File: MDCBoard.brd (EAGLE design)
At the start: 43.9 x 32.6 mm, 200 parts, among them J1 JUMPER-SOLDER, J10 MICROSD-SOCKET, J11 USB-C-RECEPTACLE-KOREANHRO, J2 JUMPER-SOLDER, J3 JUMPER-SOLDER, J4 JUMPER-SOLDER, J5 JST-SM02B-SRSS-TB, J6 JUMPER-SOLDER, J7 JUMPER-SOLDER, J8 JUMPER-SOLDER, Q1 PMOS-NEXPERIA-SOT1220, Q2 PMOS-NEXPERIA-SOT1220, Q3 PMOS-NEXPERIA-SOT1220, Q4 DIODESINC-DMG2305UX, Q5 DIODESINC-DMG2305UX, Q6 DIODESINC-DMG2305UX, Q7 DIODESINC-DMG2305UX, Q8 DIODESINC-DMG2305UX, U1 TI-TPS2116, U10 TI-TPS22919DCK, U11 TI-TPS22919DCK, U12 TI-TPS22919DCK, U13 TI-TPS22919DCK, U14 TI-MSP430FR2422IRHL, U16 TI-TXB0102, U17 PANASONIC-EKMB110711X, U18 LATTICE-ICE40HX4K-BG121, U19 WINBOND-W25Q40EW, U2 DIODESINC-AP7350, U20 NEXPERIA-74LVC1G98-OR-INV-INP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, U21 NEXPERIA-74LVC1G98-BUFFER, U22 ON-AR0330CS1C12SPKA0, U23 ALLIANCE-AS4C8M16MSA-6BIN, U24 STM-STM32F730, U25 DIODESINC-DT1446-04V-7, U26 NEXPERIA-74LVC1G98-INVERTER, U3 NEXPERIA-74LVC1G98-NOR, U4 MICROCHIP-MCP7383X, U5 NEXPERIA-74LVC1G98-INVERTER, U6 EATON-STN101, U7 TI-TPS62A01, U8 TI-TPS62A01, U9 TI-TPS62A01, X1 EPSON-FC-135, X2 SITIME-SIT8021, X3 SITIME-SIT8021

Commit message: 4 airwires
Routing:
- net VDD_A_3V3: track 88.1 -> 133.3 mm, vias 6 -> 7
- net VDD_B_2V8_IMG_SD: track 82.4 -> 78.6 mm
- net VDD_B_1V8_IMG_SD: track 86.7 -> 83.8 mm
- net ICE_IMG_CLK16MHZ: track 13.6 -> 12.9 mm

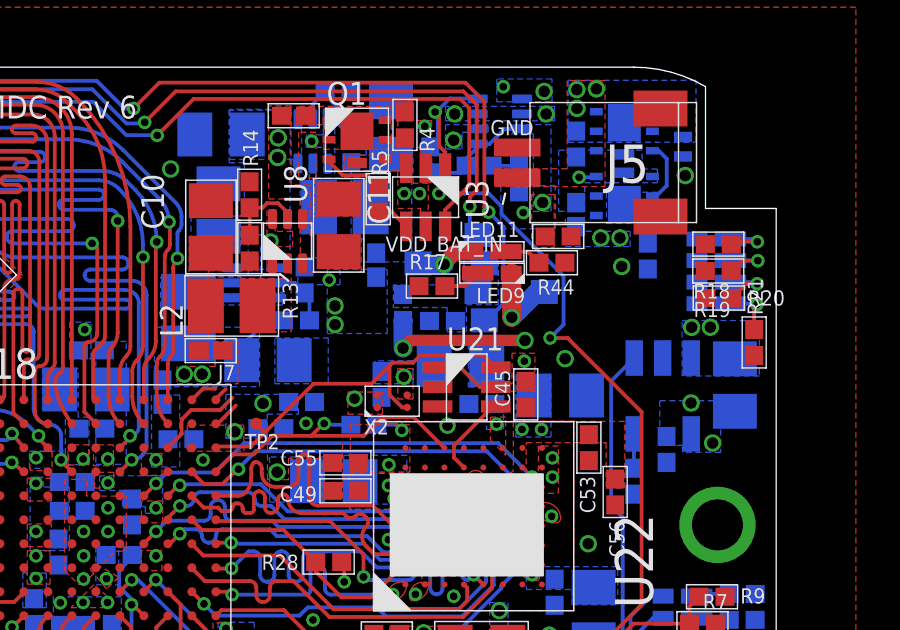
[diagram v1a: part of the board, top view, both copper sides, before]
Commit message: 0 airwires
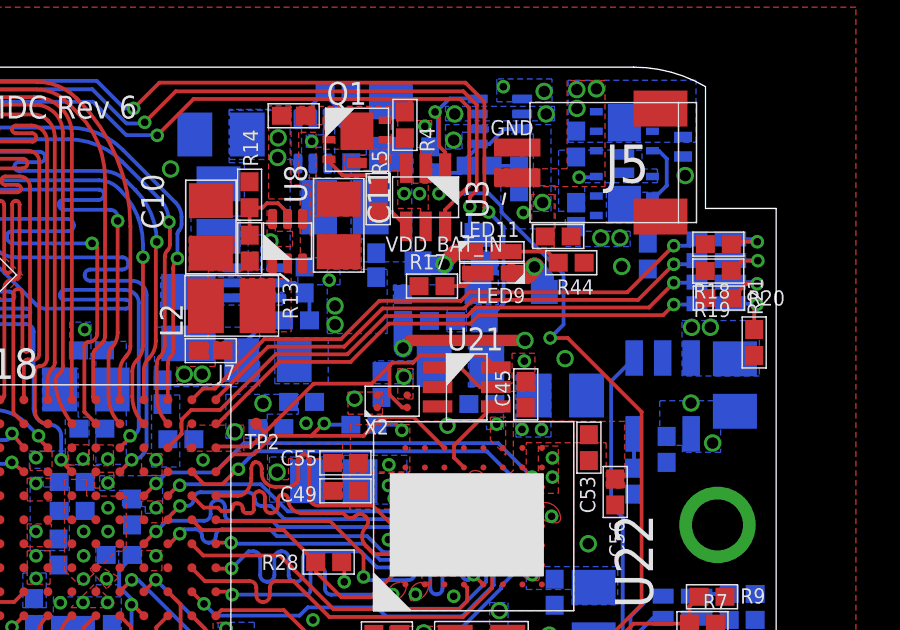
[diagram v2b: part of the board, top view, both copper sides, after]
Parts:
- moved R44 0.64 mm to (37.0, 26.1)
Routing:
- net ICE_LED0: track 0.94 -> 19.1 mm, vias 0 -> 1
- net ICE_LED1: track 0.48 -> 18.0 mm, vias 0 -> 1
- net ICE_LED2: track 3.12 -> 20.2 mm, vias 0 -> 1
- net ICE_LED3: track 0.92 -> 17.7 mm, vias 0 -> 1
- net N$6: track 2.92 -> 1.85 mm
- net VDD_USB: track 30.0 -> 30.7 mm
- net N$45: track 1.25 -> 1.90 mm

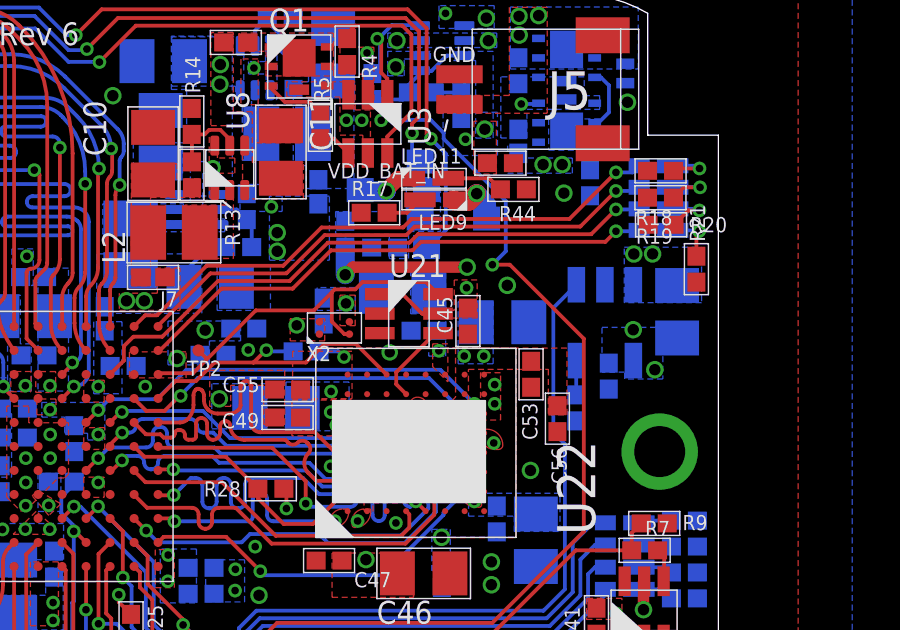
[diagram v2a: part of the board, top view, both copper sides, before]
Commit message: Moved U21 so we have more space for the o-ring to expand
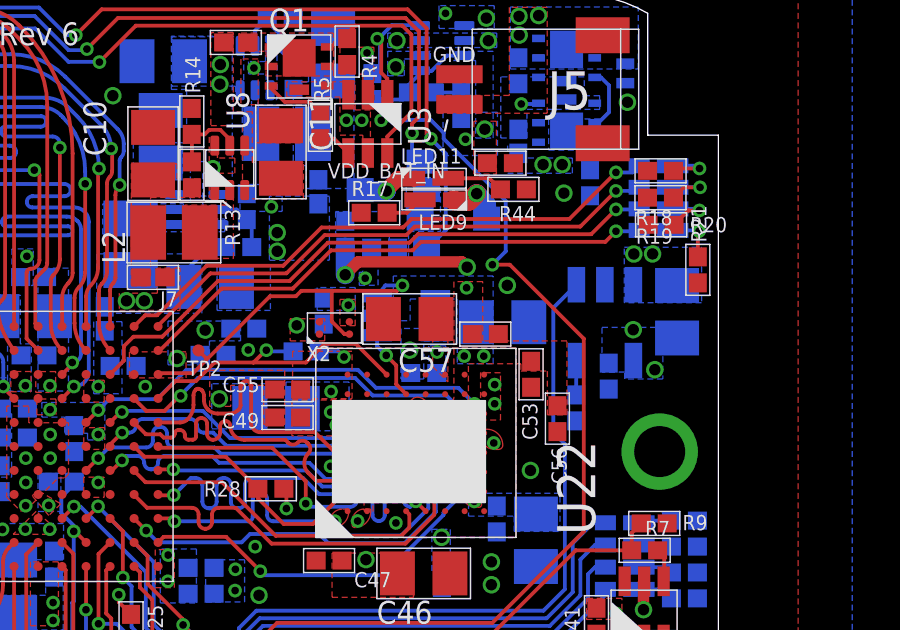
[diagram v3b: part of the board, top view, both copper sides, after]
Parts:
- moved C58 1.41 mm to (34.0, 20.0)
- moved C57 0.94 mm to (33.6, 21.8), flipped to the top, turned to 180 degrees
- moved C45 0.72 mm to (36.1, 21.3), turned to 0 degrees
- moved U21 0.11 mm to (33.5, 21.9), flipped to the bottom
- moved R21 0.05 mm to (43.2, 23.5)
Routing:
- net VDD_B_1V8_IMG_SD: track 83.8 -> 82.6 mm
- net IMG_CLK16MHZ: track 2.80 -> 2.36 mm, vias 0 -> 1
- net ICE_IMG_CLK16MHZ: track 12.9 -> 12.6 mm, vias 0 -> 1
- net GND: vias 76 -> 77

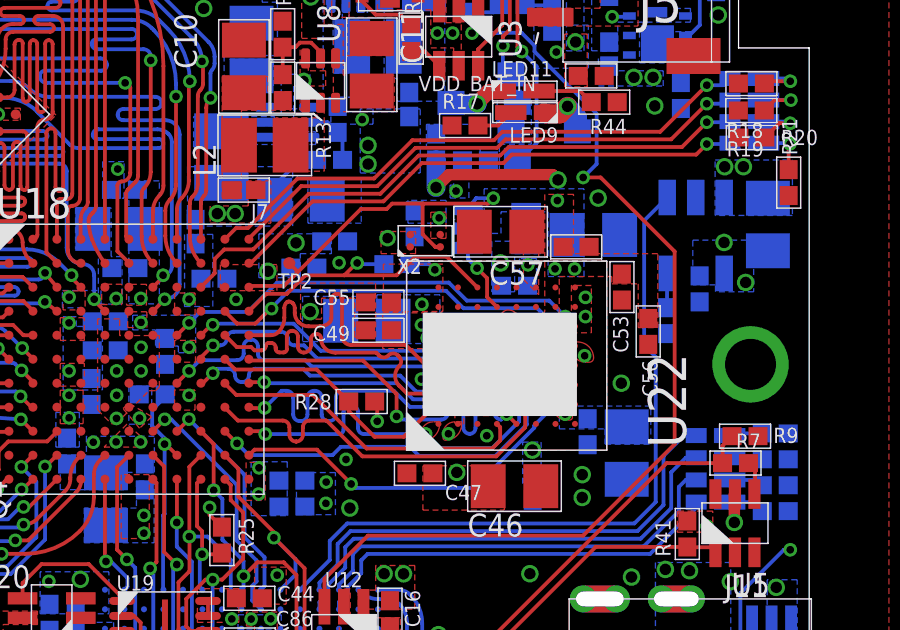
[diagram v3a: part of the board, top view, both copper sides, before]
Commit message: Make more space around lens mating circle
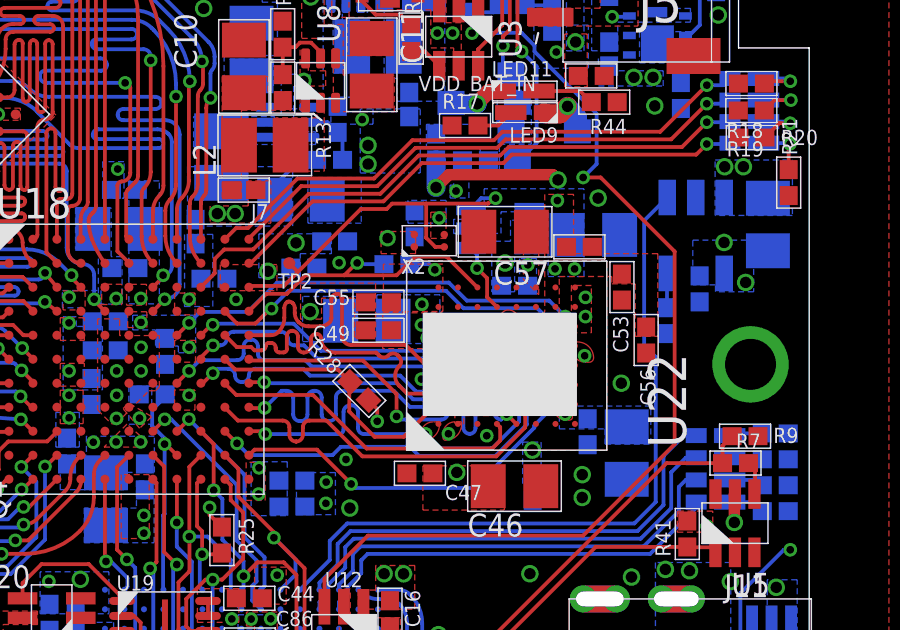
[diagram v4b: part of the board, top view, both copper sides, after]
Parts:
- moved R28 0.36 mm to (28.9, 16.5), turned to 135 degrees
- moved C56 0.30 mm to (38.4, 18.2)
- moved C57 0.15 mm to (33.7, 21.8)
- moved X2 0.13 mm to (31.2, 21.5)
- moved C45 0.11 mm to (36.2, 21.3)
- moved U21 0.10 mm to (33.6, 21.9)

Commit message: Layout progress
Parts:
- moved R7 0.25 mm to (41.7, 14.1)
- moved R9 0.25 mm to (42.0, 15.0)
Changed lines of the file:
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@@
 <attribute name="PN" value="74LVC1G98GW,125" x="41.381021875" y="12.097940625" size="1.778" layer="27" rot="R90" display="off"/>
 </element>
-<element name="R9" library="EagleLibrary" package="0402" value="300k" x="41.717096875" y="14.997796875" smashed="yes">
-<attribute name="MFG" value="Walsin" x="41.717096875" y="14.997796875" size="1.778" layer="27" display="off"/>
-<attribute name="NAME" x="42.659815625" y="14.771475" size="0.508" layer="25" font="vector"/>
-<attribute name="PN" value="WR04X3003FTL" x="41.717096875" y="14.997796875" size="1.778" layer="27" display="off"/>
+<element name="R9" library="EagleLibrary" package="0402" value="300k" x="41.971096875" y="14.997796875" smashed="yes">
+<attribute name="MFG" value="Walsin" x="41.971096875" y="14.997796875" size="1.778" layer="27" display="off"/>
+<attribute name="NAME" x="42.913815625" y="14.771475" size="0.508" layer="25" font="vector"/>
+<attribute name="PN" value="WR04X3003FTL" x="41.971096875" y="14.997796875" size="1.778" layer="27" display="off"/>
 </element>
-<element name="R7" library="EagleLibrary" package="0402" value="100k" x="41.398884375" y="14.100478125" smashed="yes" rot="R180">
-<attribute name="MFG" value="Yageo" x="41.398884375" y="14.100478125" size="1.778" layer="27" rot="R180" display="off"/>
-<attribute name="NAME" x="42.246865625" y="15.08625625" size="0.508" layer="25" font="vector" rot="R180"/>
-<attribute name="PN" value="RC0402FR-07100KL" x="41.398884375" y="14.100478125" size="1.778" layer="27" rot="R180" display="off"/>
+<element name="R7" library="EagleLibrary" package="0402" value="100k" x="41.652884375" y="14.100478125" smashed="yes" rot="R180">
+<attribute name="MFG" value="Yageo" x="41.652884375" y="14.100478125" size="1.778" layer="27" rot="R180" display="off"/>
+<attribute name="NAME" x="42.500865625" y="15.08625625" size="0.508" layer="25" font="vector" rot="R180"/>
+<attribute name="PN" value="RC0402FR-07100KL" x="41.652884375" y="14.100478125" size="1.778" layer="27" rot="R180" display="off"/>
 </element>
 <element name="C7" library="EagleLibrary" package="0402" value="100n" x="20.17004375" y="4.555859375" smashed="yes" rot="R180">
@@
 <contactref element="R7" pad="2"/>
 <wire x1="32.330146875" y1="7.3286" x2="39.102025" y2="14.100478125" width="0.127" layer="1"/>
-<wire x1="39.102025" y1="14.100478125" x2="40.966384375" y2="14.100478125" width="0.127" layer="1"/>
+<wire x1="39.102025" y1="14.100478125" x2="41.220384375" y2="14.100478125" width="0.127" layer="1"/>
 <wire x1="32.330146875" y1="4.228225" x2="28.80653125" y2="0.704609375" width="0.127" layer="1"/>
 <wire x1="32.330146875" y1="4.228225" x2="32.330146875" y2="7.3286" width="0.127" layer="1"/>
@@
 <wire x1="18.191084375" y1="0.71881875" x2="18.533978125" y2="1.0617125" width="0.127" layer="1"/>
 <wire x1="14.02161875" y1="0.71881875" x2="18.191084375" y2="0.71881875" width="0.127" layer="1"/>
-<wire x1="41.284596875" y1="14.997796875" x2="40.966384375" y2="14.679584375" width="0.127" layer="1"/>
-<wire x1="40.966384375" y1="14.679584375" x2="40.966384375" y2="14.100478125" width="0.127" layer="1"/>
+<wire x1="41.538596875" y1="14.997796875" x2="41.220384375" y2="14.679584375" width="0.127" layer="1"/>
+<wire x1="41.220384375" y1="14.679584375" x2="41.220384375" y2="14.100478125" width="0.127" layer="1"/>
 <wire x1="23.933090625" y1="0.704609375" x2="20.60254375" y2="4.03515625" width="0.127" layer="1"/>
 <wire x1="20.60254375" y1="4.03515625" x2="20.60254375" y2="4.555859375" width="0.127" layer="1"/>
@@
 <contactref element="R7" pad="1"/>
 <wire x1="42.031021875" y1="13.068340625" x2="42.049821875" y2="13.087140625" width="0.127" layer="1"/>
-<wire x1="42.049821875" y1="13.087140625" x2="42.049821875" y2="13.882040625" width="0.127" layer="1"/>
-<wire x1="42.049821875" y1="13.882040625" x2="41.831384375" y2="14.100478125" width="0.127" layer="1"/>
+<wire x1="42.049821875" y1="13.087140625" x2="42.049821875" y2="14.064915625" width="0.127" layer="1"/>
+<wire x1="42.049821875" y1="14.064915625" x2="42.085384375" y2="14.100478125" width="0.127" layer="1"/>
 </signal>
 <signal name="MSP_HOST_MODE_">

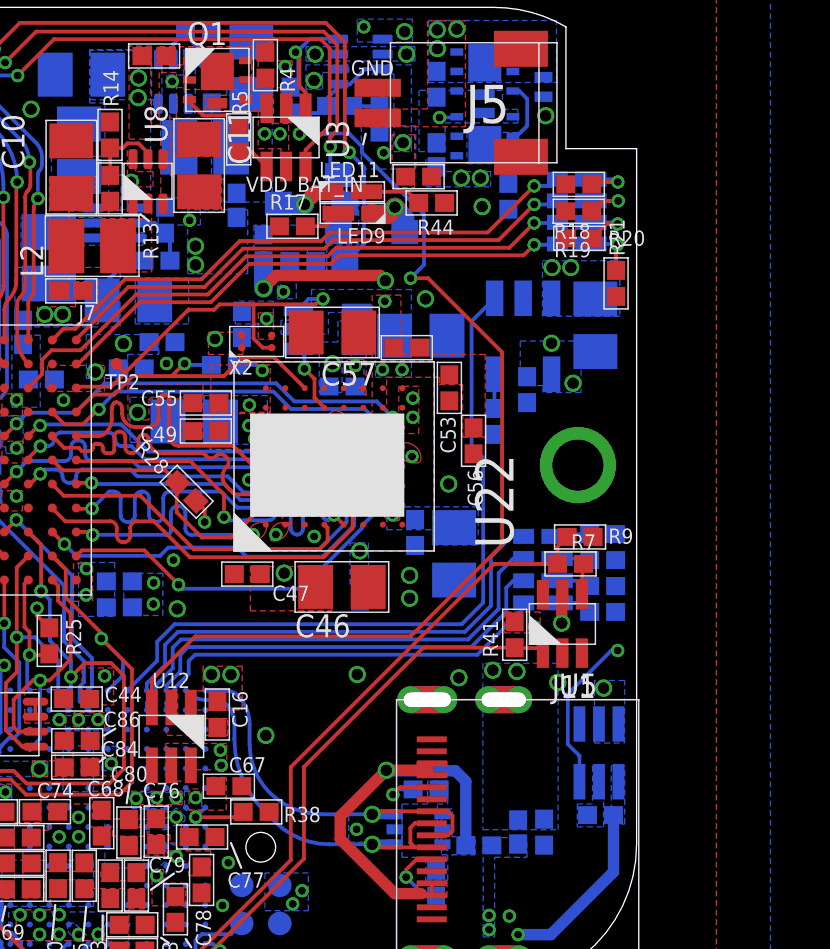
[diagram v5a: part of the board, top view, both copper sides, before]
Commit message: Move components further from lens mount ring
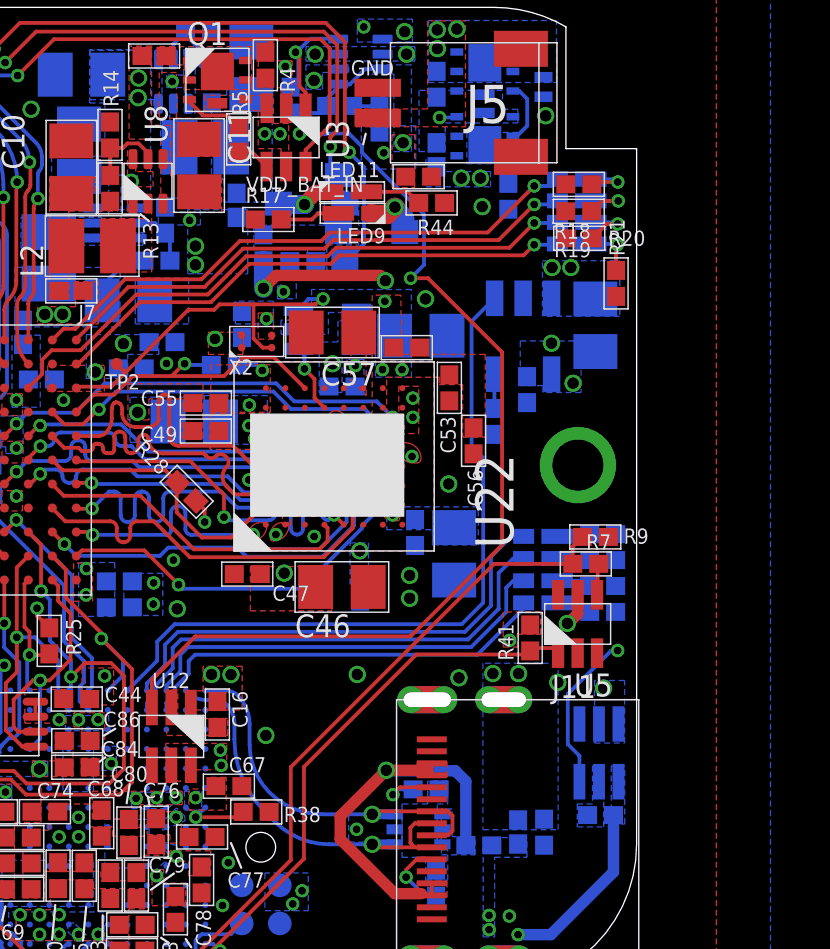
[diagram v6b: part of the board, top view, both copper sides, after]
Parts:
- moved R17 0.83 mm to (31.6, 25.6)
- moved R41 0.53 mm to (40.3, 11.6)
- moved R7 0.51 mm to (42.2, 14.1)
- moved R9 0.51 mm to (42.5, 15.0)
- moved U5 0.51 mm to (41.9, 12.1)
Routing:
- net N$16: track 1.27 -> 1.98 mm
- net BAT_CHRG_LVL: track 41.6 -> 42.1 mm
